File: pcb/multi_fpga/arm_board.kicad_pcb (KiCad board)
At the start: 2 copper layers, 208.8 x 161.7 mm, 57 parts, among them J1 PinHeader_2x06_P2.54mm_Vertic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, J2 PinHeader_1x02_P2.54mm_Vertic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, U1 Comment, U10 Comment, U11 Comment, U12 Comment, U13 Comment, U14 Comment, U15 Comment, U16 Comment, U17 Comment, U18 Comment, U19 Comment, U2 Comment, U20 Comment, U21 Comment, U22 Comment, U23 Comment, U24 Comment, U3 Comment, U4 Comment, U5 Comment, U6 Comment, U7 Comment, U8 Comment, U9 Comment

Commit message: Changed to current version of FT232H.
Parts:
- A1: footprint DIP-48_W15.24mm_Socket -> Package_DIP:DIP-48_W15.24mm_Socket
- C1, C10, C11, C12, C13, C14, C15, C16, C17, C18, C19, C2, C20, C21, C22, C23, C24, C25, C26, C3, C4, C5, C6, C7, C8, C9: footprint C_0603_1608Metric -> Capacitor_SMD:C_0603_1608Metric
- H1A: footprint MountingHole_2.7mm_M2.5 -> MountingHole:MountingHole_2.7mm_M2.5
- H1E1, H1E2: footprint MountingHole_3.2mm_M3 -> MountingHole:MountingHole_3.2mm_M3
- J1: footprint PinHeader_2x06_P2.54mm_Vertical -> Connector_PinHeader_2.54mm:PinHeader_2x06_P2.54mm_Vertical
- J2: footprint PinHeader_1x02_P2.54mm_Vertical -> Connector_PinHeader_2.54mm:PinHeader_1x02_P2.54mm_Vertical
- U1, U10, U11, U12, U13, U14, U15, U16, U17, U18, U19, U2, U20, U21, U22, U23, U24, U3, U4, U5, U6, U7, U8, U9: footprint IFX-PG-LLGA-5-4 -> IM72D128:IFX-PG-LLGA-5-4
- VR1: footprint SOT-23 -> Package_TO_SOT_SMD:SOT-23

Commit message: Flipped 6x2 recepticles to back side.
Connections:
- A1 pad 16: (no net) -> SPOKE0_D0
- A1 pad 17: (no net) -> SPOKE0_D1
- A1 pad 18: (no net) -> SPOKE0_D2
- A1 pad 19: (no net) -> SPOKE0_D3
- A1 pad 20: (no net) -> SPOKE0_D4
- A1 pad 21: (no net) -> SPOKE0_D5
- A1 pad 22: (no net) -> SPOKE0_STROBE
- A1 pad 23: (no net) -> SPOKE0_CLK
- J1 pad 1: (no net) -> SPOKE0_D0
- J1 pad 10: (no net) -> SPOKE0_CLK
- J1 pad 2: (no net) -> SPOKE0_D1
- J1 pad 3: (no net) -> SPOKE0_D2
- J1 pad 4: (no net) -> SPOKE0_D3
- J1 pad 7: (no net) -> SPOKE0_D4
- J1 pad 8: (no net) -> SPOKE0_D5
- J1 pad 9: (no net) -> SPOKE0_STROBE
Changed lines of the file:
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@@
 			(layers "*.Cu" "*.Mask")
 			(remove_unused_layers no)
+			(net "SPOKE0_D0")
 		)
 		(pad "2" thru_hole circle
@@
 			(layers "*.Cu" "*.Mask")
 			(remove_unused_layers no)
+			(net "SPOKE0_D1")
 		)
 		(pad "3" thru_hole circle
@@
 			(layers "*.Cu" "*.Mask")
 			(remove_unused_layers no)
+			(net "SPOKE0_D2")
 		)
 		(pad "4" thru_hole circle
@@
 			(layers "*.Cu" "*.Mask")
 			(remove_unused_layers no)
+			(net "SPOKE0_D3")
 		)
 		(pad "5" thru_hole circle
@@
 			(layers "*.Cu" "*.Mask")
 			(remove_unused_layers no)
+			(net "SPOKE0_D4")
 		)
 		(pad "8" thru_hole circle
@@
 			(layers "*.Cu" "*.Mask")
 			(remove_unused_layers no)
+			(net "SPOKE0_D5")
 		)
 		(pad "9" thru_hole circle
@@
 			(layers "*.Cu" "*.Mask")
 			(remove_unused_layers no)
+			(net "SPOKE0_STROBE")
 		)
 		(pad "10" thru_hole circle
@@
 			(layers "*.Cu" "*.Mask")
 			(remove_unused_layers no)
+			(net "SPOKE0_CLK")
 		)
 		(pad "11" thru_hole circle
@@
 			(layers "*.Cu" "*.Mask")
 			(remove_unused_layers no)
+			(net "SPOKE0_D0")
 		)
 		(pad "17" thru_hole circle
@@
 			(layers "*.Cu" "*.Mask")
 			(remove_unused_layers no)
+			(net "SPOKE0_D1")
 		)
 		(pad "18" thru_hole circle
@@
 			(layers "*.Cu" "*.Mask")
 			(remove_unused_layers no)
+			(net "SPOKE0_D2")
 		)
 		(pad "19" thru_hole circle
@@
 			(layers "*.Cu" "*.Mask")
 			(remove_unused_layers no)
+			(net "SPOKE0_D3")
 		)
 		(pad "20" thru_hole circle
@@
 			(layers "*.Cu" "*.Mask")
 			(remove_unused_layers no)
+			(net "SPOKE0_D4")
 		)
 		(pad "21" thru_hole circle
@@
 			(layers "*.Cu" "*.Mask")
 			(remove_unused_layers no)
+			(net "SPOKE0_D5")
 		)
 		(pad "22" thru_hole circle
@@
 			(layers "*.Cu" "*.Mask")
 			(remove_unused_layers no)
+			(net "SPOKE0_STROBE")
 		)
 		(pad "23" thru_hole circle
@@
 			(layers "*.Cu" "*.Mask")
 			(remove_unused_layers no)
+			(net "SPOKE0_CLK")
 		)
 		(pad "24" thru_hole circle

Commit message: Fixed locations of power and spoke connectors.
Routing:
- net GND: track 697.6 -> 685.9 mm
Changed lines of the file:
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@@
-	)
-	(segment
-		(start 153.8773 59.5392)
-		(end 147.7385 59.5392)
-		(width 0.25)
-		(layer "F.Cu")
-		(net "GND")
 	)
 	(segment
@@
 	)
 	(segment
-		(start 156.5135 62.1754)
-		(end 153.8773 59.5392)
-		(width 0.25)
-		(layer "F.Cu")
-		(net "GND")
-	)
-	(segment
 		(start 113.9031 42.437)
 		(end 113.9031 44.04)
@@
 		(start 137.9985 155.7048)
 		(end 138.0095 155.6938)
-		(width 0.25)
-		(layer "F.Cu")
-		(net "GND")
-	)
-	(segment
-		(start 147.7385 59.5392)
-		(end 146.4418 58.2425)
 		(width 0.25)
 		(layer "F.Cu")
@@
 		(min_thickness 0.25)
 		(fill yes
-			(thermal_gap 0.5)
-			(thermal_bridge_width 0.5)
+			(thermal_gap 0.2)
+			(thermal_bridge_width 0.25)
 			(island_removal_mode 0)
 		)
@@
 				(xy 130.748902 28.422119) (xy 127.172972 27.307867) (xy 123.867104 26.406834) (xy 120.81515 25.691847)
 				(xy 118.001451 25.138594) (xy 115.410891 24.725365) (xy 113.028939 24.432808) (xy 110.84167 24.24371)
+				(xy 108.835791 24.142791)
 			)
 		)

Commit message: Hand-routed.
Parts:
- moved C26 11.0 mm to (157.0, 60.5)
- moved C25 8.14 mm to (152.5, 54.7), turned to 90 degrees
- moved VR1 5.74 mm to (156.0, 57.0)
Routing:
- net GND: track 685.9 -> 29.1 mm, vias 9 -> 0
- net SPOKE0_D2: track 0.00 -> 106.1 mm, vias 0 -> 1
- net SPOKE0_D4: track 0.00 -> 106.0 mm, vias 0 -> 1
- net SPOKE0_STROBE: track 0.00 -> 105.2 mm, vias 0 -> 1
- net SPOKE0_CLK: track 0.00 -> 102.7 mm
- net SPOKE0_D3: track 0.00 -> 100.6 mm, vias 0 -> 1
- net SPOKE0_D5: track 0.00 -> 99.3 mm
- net SPOKE0_D0: track 0.00 -> 98.2 mm, vias 0 -> 1
- net SPOKE0_D1: track 0.00 -> 95.4 mm, vias 0 -> 1
- net DATA_08: track 101.7 -> 123.6 mm, vias 1 -> 2
- net DATA_04: track 85.6 -> 105.3 mm, vias 2 -> 3
- net DATA_07: track 70.6 -> 89.3 mm
- net DATA_02: track 62.2 -> 46.0 mm, vias 0 -> 2
- net DATA_00: track 94.8 -> 104.1 mm, vias 2 -> 3
- net +5V: track 119.5 -> 126.5 mm
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
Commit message: Finished hand-routing. DRC-clean.
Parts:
- moved C1 0.11 mm to (114.5, 28.0)
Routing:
- net C0_PDM_CLK: track 618.6 -> 624.8 mm, vias 23 -> 25
- net DATA_09: track 95.5 -> 100.2 mm, vias 0 -> 2
- net DATA_05: track 56.3 -> 59.4 mm
- net DATA_03: track 61.0 -> 63.6 mm, vias 0 -> 3
- net C0_1V8: track 626.6 -> 624.7 mm, vias 7 -> 15
- net +5V: track 126.5 -> 124.9 mm

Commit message: Cleaned up.
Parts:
- moved C6 0.68 mm to (183.5, 93.5)
- moved C15 0.57 mm to (137.9, 150.5)
- moved C7 0.55 mm to (193.3, 110.0)
- moved C10 0.53 mm to (121.2, 56.5)
- moved C20 0.51 mm to (94.4, 106.0)
- moved C5 0.50 mm to (172.5, 78.0)
- moved C11 0.46 mm to (128.2, 74.5)
- moved C18 0.46 mm to (102.5, 68.5)
- moved C8 0.44 mm to (202.0, 127.0)
- moved C22 0.41 mm to (79.2, 141.5)
- moved C3 0.40 mm to (146.5, 49.0)
- moved C2 0.36 mm to (131.5, 37.0)
- moved C14 0.32 mm to (137.5, 131.5)
- moved C4 0.29 mm to (160.0, 63.0)
- moved C24 0.29 mm to (60.0, 175.0)
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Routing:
- net C0_1V8: track 624.7 -> 84.1 mm, vias 15 -> 18
- net GND: track 29.1 -> 152.4 mm, vias 0 -> 46
- net C0_PDM_CLK: track 624.8 -> 619.8 mm
- net DATA_04: track 105.3 -> 109.9 mm
- net DATA_08: track 123.6 -> 127.7 mm, vias 2 -> 0
- net DATA_11: track 125.4 -> 128.1 mm, vias 2 -> 0
- net DATA_06: track 45.4 -> 46.5 mm
- net DATA_10: track 98.4 -> 99.4 mm
- net DATA_00: track 104.1 -> 104.7 mm, vias 3 -> 0
- net DATA_05: track 59.4 -> 58.8 mm
- net DATA_07: track 89.3 -> 88.7 mm
- net DATA_09: track 100.2 -> 100.0 mm, vias 2 -> 0
- added copper zone on In2.Cu, net C0_1V8
- added copper zone on In1.Cu, net GND
- removed copper zone on F.Cu, net GND
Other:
- copper layers 2 -> 4

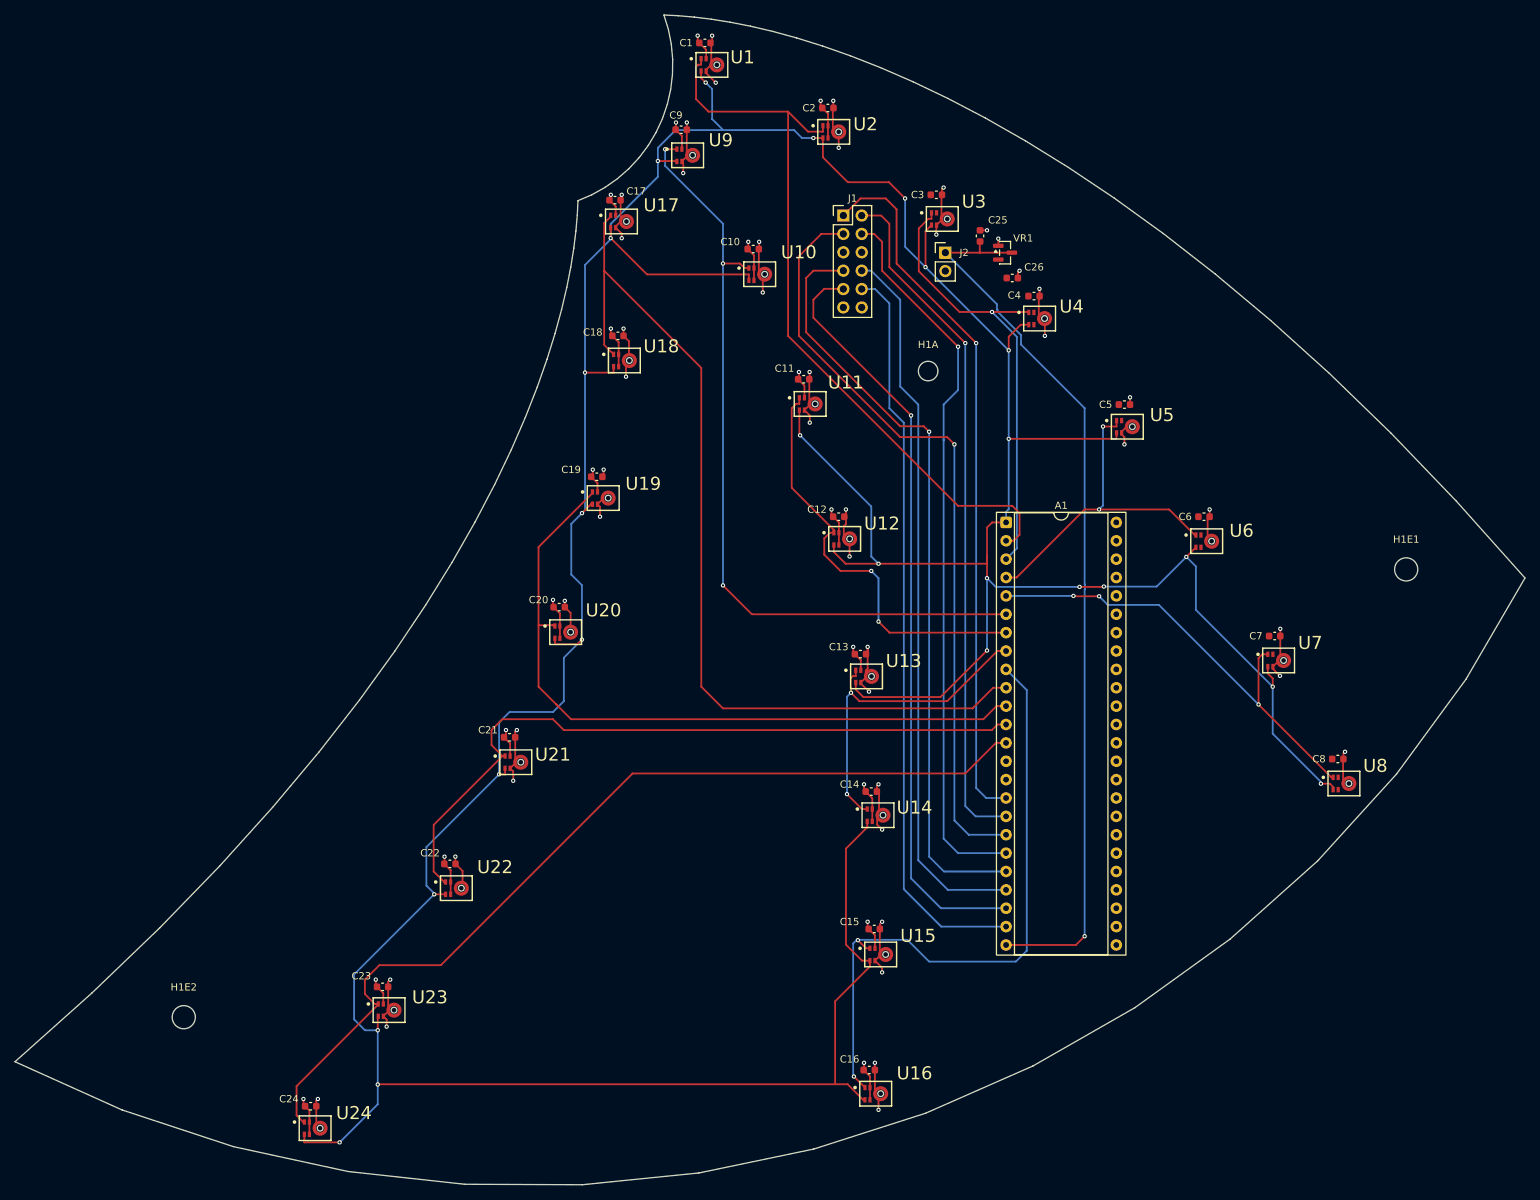
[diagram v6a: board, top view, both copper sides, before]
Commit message: Removed clock and data, rerouted bus and power.
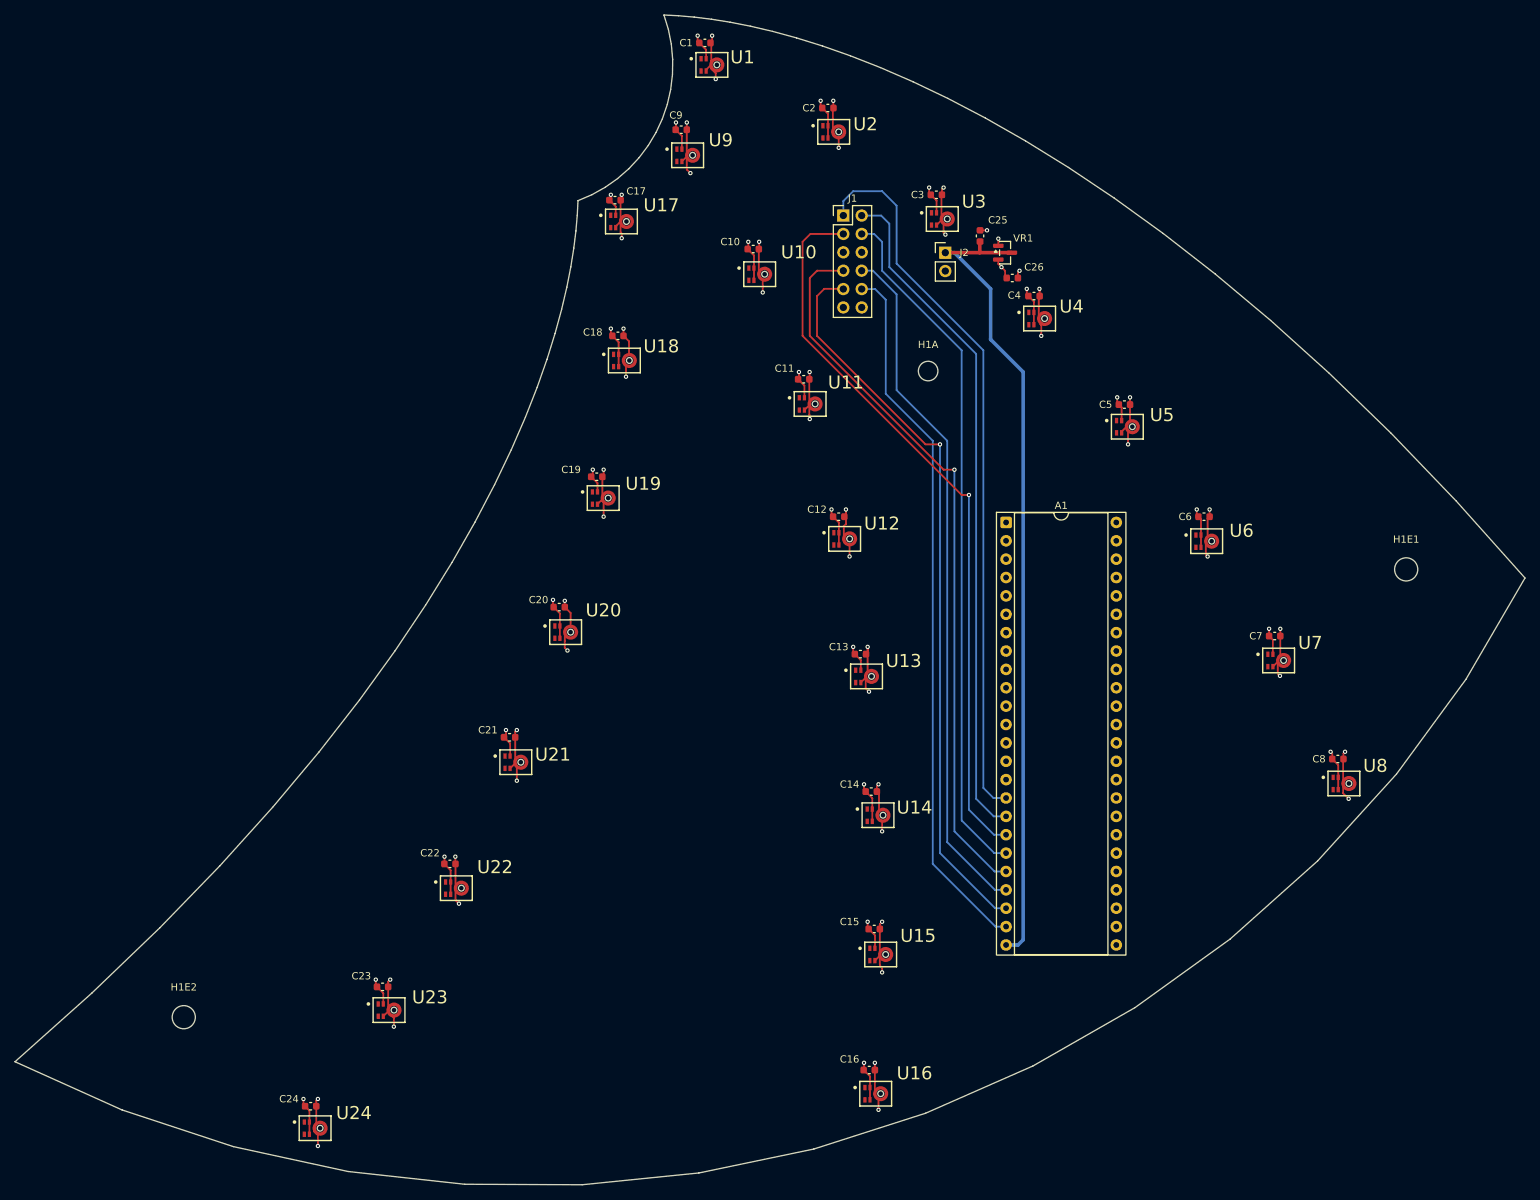
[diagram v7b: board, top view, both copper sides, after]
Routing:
- net C0_PDM_CLK: track 619.8 -> 0.00 mm, vias 25 -> 0
- net DATA_11: track 128.1 -> 0.00 mm
- net DATA_08: track 127.7 -> 0.00 mm
- net DATA_04: track 109.9 -> 0.00 mm, vias 3 -> 0
- net DATA_00: track 104.7 -> 0.00 mm
- net DATA_09: track 100.0 -> 0.00 mm
- net DATA_10: track 99.4 -> 0.00 mm
- net DATA_07: track 88.7 -> 0.00 mm, vias 2 -> 0
- net DATA_03: track 63.6 -> 0.00 mm, vias 3 -> 0
- net DATA_01: track 62.8 -> 0.00 mm, vias 1 -> 0
- net DATA_05: track 58.8 -> 0.00 mm, vias 2 -> 0
- net DATA_06: track 46.5 -> 0.00 mm, vias 2 -> 0
- net DATA_02: track 46.0 -> 0.00 mm, vias 2 -> 0
- net C0_1V8: track 84.1 -> 114.8 mm, vias 18 -> 25
- net GND: track 152.4 -> 180.1 mm, vias 46 -> 51
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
